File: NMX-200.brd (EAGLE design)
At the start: 67.3 x 63.5 mm, 92 parts, among them IC1 AT90USB1287-AU, J1 PJ-002AH, J3 SJ1-2503A, J4 RJHSE-5385-02, J5 SJ1-2503A, J6 SJ1-2503A, Q1 P-CHANNEL_MOSFET, T1 CMPT2369, T2 CMPT2369, T3 CMPT2369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

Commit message: Added fiducials to bottom of NMX-200
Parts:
- added U$6, U$7: FIDUCIAL, adafruit:FIDUCIAL_1MM
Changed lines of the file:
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@@
 <setting verticaltext="up"/>
 </settings>
-<grid distance="1" unitdist="mm" unit="mm" style="lines" multiple="1" display="yes" altdistance="5" altunitdist="mil" altunit="mil"/>
+<grid distance="0.01" unitdist="inch" unit="mil" style="lines" multiple="1" display="yes" altdistance="5" altunitdist="mil" altunit="mil"/>
 <layers>
 <layer number="1" name="Top" color="4" fill="1" visible="yes" active="yes"/>
-<layer number="2" name="Route2" color="1" fill="3" visible="no" active="yes"/>
+<layer number="2" name="Route2" color="1" fill="3" visible="yes" active="yes"/>
 <layer number="3" name="Route3" color="4" fill="3" visible="no" active="no"/>
 <layer number="14" name="Route14" color="1" fill="6" visible="no" active="no"/>
-<layer number="15" name="Route15" color="4" fill="6" visible="no" active="yes"/>
+<layer number="15" name="Route15" color="4" fill="6" visible="yes" active="yes"/>
 <layer number="16" name="Bottom" color="1" fill="1" visible="yes" active="yes"/>
 <layer number="17" name="Pads" color="2" fill="1" visible="yes" active="yes"/>
@@
 </element>
 <element name="U$5" library="dynamic_perception" package="10118194-0001LF" value="USB_CONN" x="65.405" y="34.29" rot="R90"/>
+<element name="U$6" library="adafruit" package="FIDUCIAL_1MM" value="FIDUCIAL" x="58.42" y="16.51" rot="MR0"/>
+<element name="U$7" library="adafruit" package="FIDUCIAL_1MM" value="FIDUCIAL" x="2.54" y="60.96" rot="MR0"/>
 </elements>
 <signals>
@@
 <wire x1="3.49" y1="31.67" x2="3.49" y2="30.414" width="0.3048" layer="1"/>
 <wire x1="3.49" y1="30.414" x2="2.54" y2="29.464" width="0.3048" layer="1"/>
-<wire x1="2.54" y1="29.464" x2="1.016" y2="29.464" width="0.3048" layer="1"/>
-<wire x1="1.016" y1="29.464" x2="0.762" y2="28.956" width="0.3048" layer="1"/>
-<wire x1="0.762" y1="28.956" x2="0.762" y2="23.368" width="0.3048" layer="1"/>
-<wire x1="0.762" y1="23.368" x2="1.016" y2="22.86" width="0.3048" layer="1"/>
-<wire x1="2.54" y1="22.708" x2="1.016" y2="22.86" width="0.3048" layer="1"/>
+<wire x1="2.54" y1="29.464" x2="1.397" y2="29.464" width="0.3048" layer="1"/>
+<wire x1="1.397" y1="29.464" x2="1.143" y2="29.083" width="0.3048" layer="1"/>
+<wire x1="1.143" y1="29.083" x2="1.143" y2="22.733" width="0.3048" layer="1"/>
+<wire x1="2.54" y1="22.708" x2="1.143" y2="22.733" width="0.3048" layer="1"/>
 <polygon width="0.6096" layer="1" thermals="no">
-<vertex x="1.016" y="21.336"/>
-<vertex x="1.524" y="20.828"/>
+<vertex x="1.27" y="20.828"/>
 <vertex x="4.572" y="20.828"/>
 <vertex x="6.096" y="19.812"/>
@@
 <vertex x="6.604" y="22.86"/>
 <vertex x="5.588" y="23.876"/>
-<vertex x="1.524" y="23.876"/>
-<vertex x="1.016" y="23.368"/>
+<vertex x="1.27" y="23.876"/>
 </polygon>
 <via x="10.16" y="19.812" extent="1-16" drill="0.254"/>
@@
 <contactref element="U15" pad="4"/>
 <polygon width="0.4064" layer="1" thermals="no">
-<vertex x="1.524" y="24.638"/>
+<vertex x="1.778" y="24.638"/>
 <vertex x="7.62" y="24.638"/>
 <vertex x="7.62" y="28.956"/>
-<vertex x="1.524" y="28.956"/>
+<vertex x="1.778" y="28.956"/>
 </polygon>
 <wire x1="3.49" y1="34.37" x2="4.746" y2="34.37" width="0.3048" layer="1"/>
@@
 </signal>
 <signal name="N$16">
-<polygon width="0.4064" layer="16" pour="cutout">
+<polygon width="0.4064" layer="16">
 <vertex x="56" y="1"/>
 <vertex x="67" y="1"/>

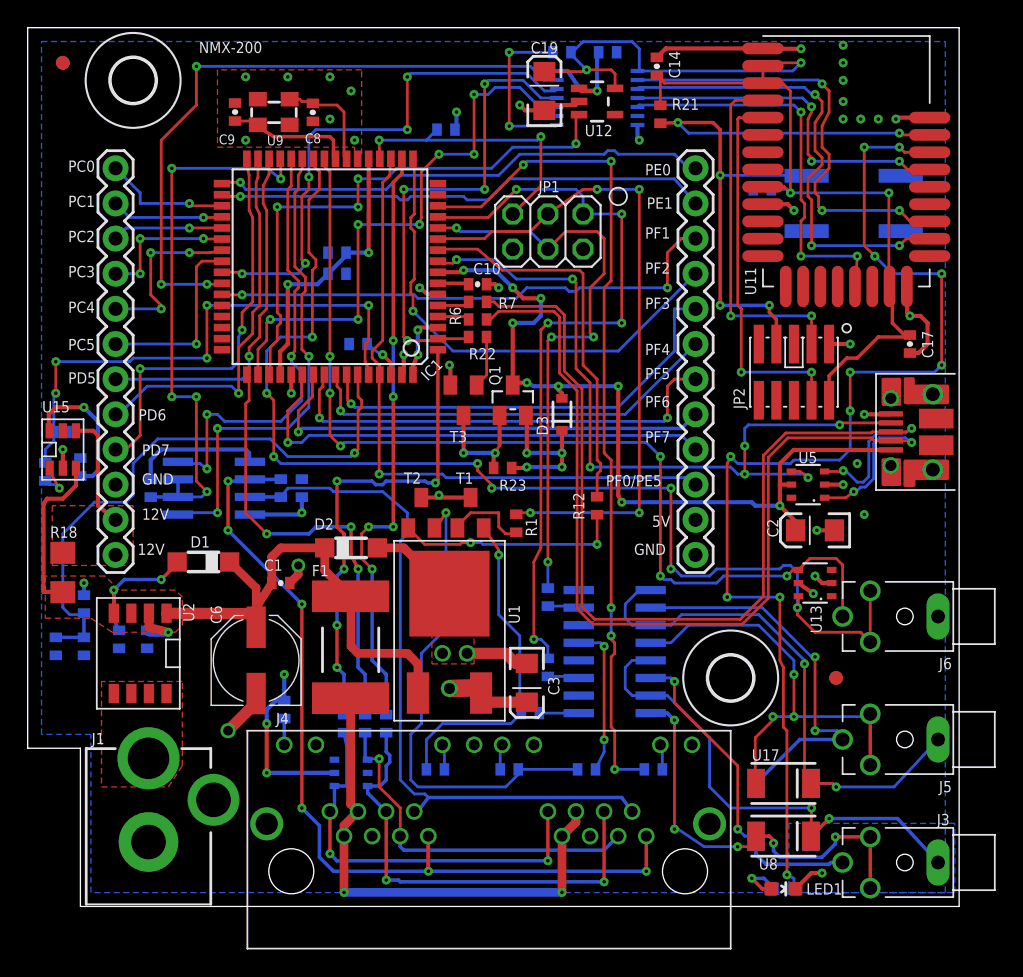
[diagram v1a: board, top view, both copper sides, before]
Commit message: Fixed some ERC errors, switched to OSHPark DRC
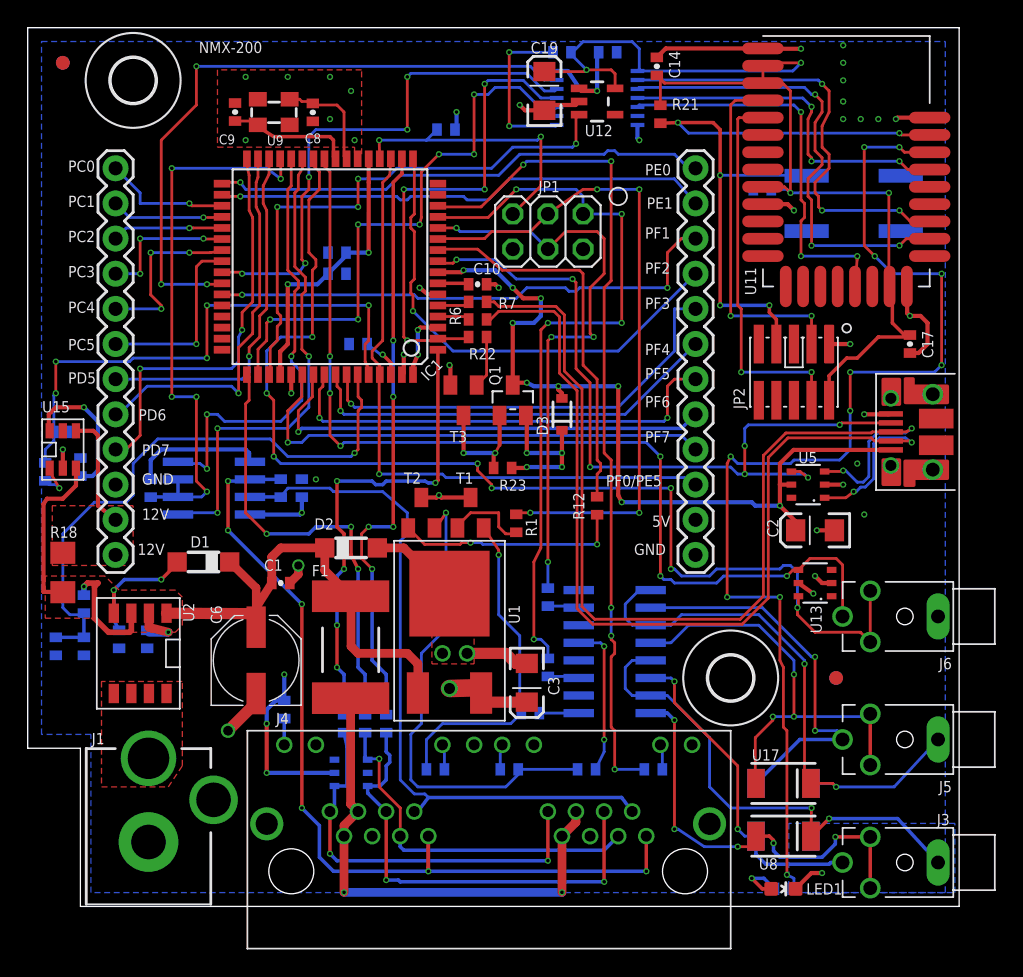
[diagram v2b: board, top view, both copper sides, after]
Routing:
- net 12V: track 52.4 -> 60.3 mm
- net GND: vias 38 -> 39
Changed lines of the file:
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@@
 <layers>
 <layer number="1" name="Top" color="4" fill="1" visible="yes" active="yes"/>
-<layer number="2" name="Route2" color="1" fill="3" visible="yes" active="yes"/>
+<layer number="2" name="Route2" color="1" fill="3" visible="no" active="yes"/>
 <layer number="3" name="Route3" color="4" fill="3" visible="no" active="no"/>
 <layer number="14" name="Route14" color="1" fill="6" visible="no" active="no"/>
-<layer number="15" name="Route15" color="4" fill="6" visible="yes" active="yes"/>
-<layer number="16" name="Bottom" color="1" fill="1" visible="yes" active="yes"/>
+<layer number="15" name="Route15" color="4" fill="6" visible="no" active="yes"/>
+<layer number="16" name="Bottom" color="1" fill="1" visible="no" active="yes"/>
 <layer number="17" name="Pads" color="2" fill="1" visible="yes" active="yes"/>
 <layer number="18" name="Vias" color="2" fill="1" visible="yes" active="yes"/>
@@
 </class>
 </classes>
-<designrules name="SSC-EAGLE-4Lyr_v1.0.0.3 *">
-<description language="en">&lt;b&gt;EAGLE Design Rules for *4* Layer Designs (MLB)&lt;/b&gt;
+<designrules name="OSHPark-4layer">
+<description language="de">&lt;b&gt;EAGLE Design Rules&lt;/b&gt;
 &lt;p&gt;
-This Sunstone Circuits 4 Layer .DRU has been set to cover our minimum requirements for our 4 layer MLB products. For questions, comments, suggestions, please contact Sunstone Customer Support:&lt;p&gt;&lt;b&gt;Email:&lt;/b&gt; mailto:support@sunstone.com&lt;b&gt;&lt;br&gt;Phone:&lt;/b&gt; 800-228-8198&lt;p&gt; v1.1Mod10/16/07~Layers-core reversal.Distance C/D.Restring%.Supply G
-&lt;p&gt;v1.2Mod12/06/07~Distance C/D to 20mils.&lt;p&gt;v1.3Mod12/12/07~Supply/Annulus Value to 12.5mils&lt;p&gt;1/15/08 SSC-EAGLE-4Lyr_v1.0.0.3~For Release&lt;p&gt;10/03/08 Description Edit&lt;p&gt;
-&lt;i&gt;Attention: Upon running the design check and making modifications, please remember to save any changes before closing the application and sending in your board file to Sunstone Circuits for conversion.&lt;i&gt;</description>
-<param name="layerSetup" value="(1+2*15+16)"/>
-<param name="mtCopper" value="0.0178mm 0.0356mm 0.0356mm 0.0356mm 0.0356mm 0.0356mm 0.0356mm 0.0356mm 0.0356mm 0.0356mm 0.0356mm 0.0356mm 0.0356mm 0.0356mm 0.0356mm 0.0178mm"/>
-<param name="mtIsolate" value="12mil 28mil 12mil 0.1499mm 0.2007mm 0.1499mm 0.2007mm 0.1499mm 0.2007mm 0.1499mm 0.2007mm 0.1499mm 0.2007mm 0.1499mm 12mil"/>
-<param name="mdWireWire" value="6mil"/>
-<param name="mdWirePad" value="6mil"/>
-<param name="mdWireVia" value="6mil"/>
-<param name="mdPadPad" value="6mil"/>
-<param name="mdPadVia" value="6mil"/>
-<param name="mdViaVia" value="6mil"/>
-<param name="mdSmdPad" value="6mil"/>
-<param name="mdSmdVia" value="6mil"/>
-<param name="mdSmdSmd" value="6mil"/>
+Die Standard-Design-Rules sind so gewählt, dass sie für
+die meisten Anwendungen passen. Sollte ihre Platine
+besondere Anforderungen haben, treffen Sie die erforderlichen
+Einstellungen hier und speichern die Design Rules unter
+einem neuen Namen ab.</description>
+<description language="en">&lt;b&gt;Laen's PCB Order Design Rules&lt;/b&gt;
+&lt;p&gt;
+Please make sure your boards conform to these design rules.</description>
+<param name="layerSetup" value="(1*2*15*16)"/>
+<param name="mtCopper" value="0.035559375mm 0.01778125mm 0.0356mm 0.0356mm 0.0356mm 0.0356mm 0.0356mm 0.0356mm 0.0356mm 0.0356mm 0.0356mm 0.0356mm 0.0356mm 0.0356mm 0.01778125mm 0.035559375mm"/>
+<param name="mtIsolate" value="0.17018125mm 47mil 0.2007mm 0.1499mm 0.2007mm 0.1499mm 0.2007mm 0.1499mm 0.2007mm 0.1499mm 0.2007mm 0.1499mm 0.2007mm 0.1499mm 0.17018125mm"/>
+<param name="mdWireWire" value="5mil"/>
+<param name="mdWirePad" value="5mil"/>
+<param name="mdWireVia" value="5mil"/>
+<param name="mdPadPad" value="5mil"/>
+<param name="mdPadVia" value="5mil"/>
+<param name="mdViaVia" value="5mil"/>
+<param name="mdSmdPad" value="5mil"/>
+<param name="mdSmdVia" value="5mil"/>
+<param name="mdSmdSmd" value="5mil"/>
 <param name="mdViaViaSameLayer" value="8mil"/>
 <param name="mnLayersViaInSmd" value="2"/>
-<param name="mdCopperDimension" value="20mil"/>
-<param name="mdDrill" value="16mil"/>
+<param name="mdCopperDimension" value="15mil"/>
+<param name="mdDrill" value="6mil"/>
 <param name="mdSmdStop" value="0mil"/>
-<param name="msWidth" value="6mil"/>
-<param name="msDrill" value="8mil"/>
-<param name="msMicroVia" value="9.9898mm"/>
+<param name="msWidth" value="5mil"/>
+<param name="msDrill" value="10mil"/>
+<param name="msMicroVia" value="10mil"/>
 <param name="msBlindViaRatio" value="0.5"/>
 <param name="rvPadTop" value="0.25"/>
@@
 <param name="rvMicroViaOuter" value="0.25"/>
 <param name="rvMicroViaInner" value="0.25"/>
-<param name="rlMinPadTop" value="8mil"/>
-<param name="rlMaxPadTop" value="999mil"/>
-<param name="rlMinPadInner" value="8mil"/>
-<param name="rlMaxPadInner" value="999mil"/>
-<param name="rlMinPadBottom" value="8mil"/>
-<param name="rlMaxPadBottom" value="999mil"/>
-<param name="rlMinViaOuter" value="8mil"/>
-<param name="rlMaxViaOuter" value="999mil"/>
-<param name="rlMinViaInner" value="8mil"/>
-<param name="rlMaxViaInner" value="999mil"/>
-<param name="rlMinMicroViaOuter" value="8mil"/>
-<param name="rlMaxMicroViaOuter" value="999mil"/>
-<param name="rlMinMicroViaInner" value="8mil"/>
-<param name="rlMaxMicroViaInner" value="999mil"/>
+<param name="rlMinPadTop" value="4mil"/>
+<param name="rlMaxPadTop" value="20mil"/>
+<param name="rlMinPadInner" value="4mil"/>
+<param name="rlMaxPadInner" value="20mil"/>
+<param name="rlMinPadBottom" value="4mil"/>
+<param name="rlMaxPadBottom" value="20mil"/>
+<param name="rlMinViaOuter" value="4mil"/>
+<param name="rlMaxViaOuter" value="20mil"/>
+<param name="rlMinViaInner" value="4mil"/>
+<param name="rlMaxViaInner" value="20mil"/>
+<param name="rlMinMicroViaOuter" value="4mil"/>
+<param name="rlMaxMicroViaOuter" value="20mil"/>
+<param name="rlMinMicroViaInner" value="4mil"/>
+<param name="rlMaxMicroViaInner" value="20mil"/>
 <param name="psTop" value="-1"/>
 <param name="psBottom" value="-1"/>
@@
 <param name="mvStopFrame" value="1"/>
 <param name="mvCreamFrame" value="0"/>
-<param name="mlMinStopFrame" value="3mil"/>
-<param name="mlMaxStopFrame" value="3mil"/>
+<param name="mlMinStopFrame" value="2.5mil"/>
+<param name="mlMaxStopFrame" value="2.5mil"/>
 <param name="mlMinCreamFrame" value="0mil"/>
 <param name="mlMaxCreamFrame" value="0mil"/>
-<param name="mlViaStopLimit" value="11mil"/>
+<param name="mlViaStopLimit" value="0mil"/>
 <param name="srRoundness" value="0"/>
 <param name="srMinRoundness" value="0mil"/>
@@
 <param name="checkFont" value="1"/>
 <param name="checkRestrict" value="1"/>
-<param name="useDiameter" value="31"/>
+<param name="useDiameter" value="13"/>
 <param name="maxErrors" value="50"/>
 </designrules>
@@
 <wire x1="16.002" y1="32.766" x2="16.002" y2="32.191" width="0.3048" layer="16"/>
 <wire x1="16.002" y1="32.191" x2="16.062" y2="32.131" width="0.3048" layer="16"/>
-<polygon width="0.3048" layer="16">
+<polygon width="0.3048" layer="16" rank="2">
 <vertex x="1" y="62.5"/>
 <vertex x="66.31" y="62.5"/>
@@
 <wire x1="65.024" y1="42.164" x2="64.516" y2="42.672" width="0.3048" layer="1"/>
 <wire x1="64.516" y1="42.672" x2="63.754" y2="42.672" width="0.3048" layer="1"/>
-<wire x1="19.812" y1="30.876" x2="16.062" y2="32.131" width="0" layer="19" extent="16-16"/>
+<via x="20.828" y="30.861" extent="1-16" drill="0.254"/>
 </signal>
 <signal name="12V" class="3">
@@
 <wire x1="17.638" y1="25.258" x2="18.288" y2="25.908" width="0.635" layer="1"/>
 <wire x1="18.288" y1="25.908" x2="21.468" y2="25.908" width="0.635" layer="1"/>
-<wire x1="4.064" y1="22.494" x2="4.064" y2="23.368" width="0.3048" layer="16"/>
-<via x="4.064" y="23.368" extent="1-16" drill="0.254" diameter="0.0254"/>
-<wire x1="7.493" y1="21.188" x2="4.064" y2="22.494" width="0" layer="19" extent="1-16"/>
+<wire x1="4.064" y1="22.494" x2="4.064" y2="23.114" width="0.4064" layer="16"/>
+<via x="4.064" y="23.114" extent="1-16" drill="0.254"/>
+<wire x1="7.493" y1="21.188" x2="7.493" y2="19.939" width="0.4064" layer="1"/>
+<wire x1="7.493" y1="19.939" x2="7.366" y2="19.812" width="0.4064" layer="1"/>
+<wire x1="7.366" y1="19.812" x2="5.842" y2="19.812" width="0.4064" layer="1"/>
+<wire x1="5.842" y1="19.812" x2="4.826" y2="20.828" width="0.4064" layer="1"/>
+<wire x1="4.826" y1="20.828" x2="4.826" y2="23.114" width="0.4064" layer="1"/>
+<wire x1="4.826" y1="23.114" x2="5.08" y2="23.368" width="0.4064" layer="1"/>
+<wire x1="5.08" y1="23.368" x2="4.318" y2="23.368" width="0.4064" layer="1"/>
+<wire x1="4.318" y1="23.368" x2="4.064" y2="23.114" width="0.4064" layer="1"/>
 </signal>
 <signal name="OK_SHT">
